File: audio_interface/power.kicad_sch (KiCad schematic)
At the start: 50 parts, among them J3 EXT_9V, J4 PROBE_GND, J5 EXT_5VA, J6 EXT_INV, J7 EXT_ANALOG, J8 D_PWR_SEL, J9 EXT_DIGITAL, U5 L4931, U6 LT1931, U7 TPS7A49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

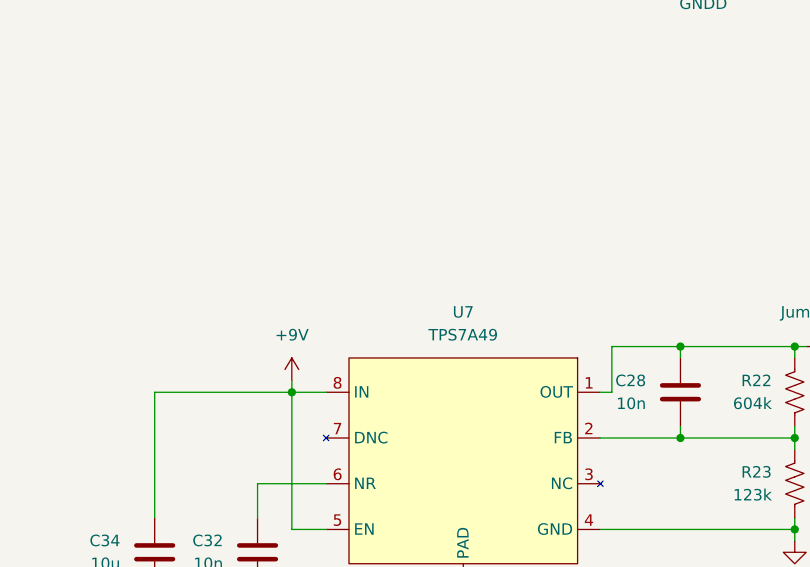
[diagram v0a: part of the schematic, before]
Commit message: Fixed some footprints, fixed silkscreen.
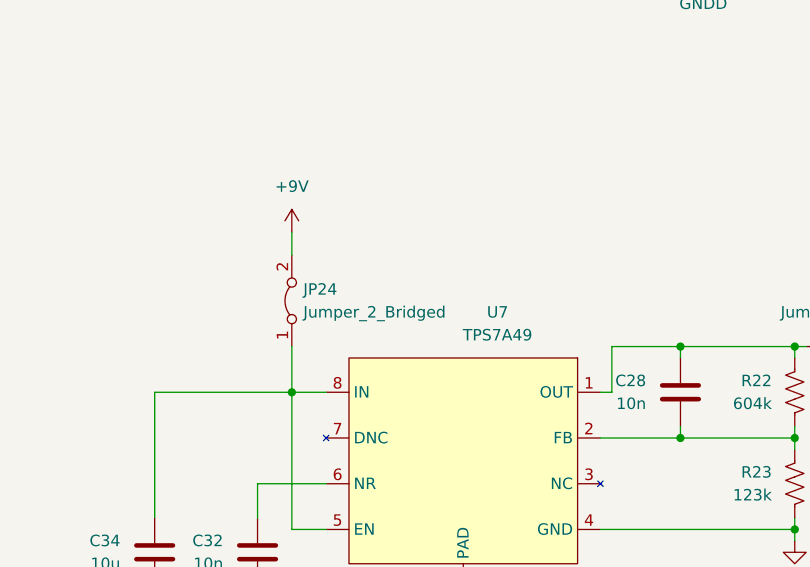
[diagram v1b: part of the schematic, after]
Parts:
- added JP24: Jumper_2_Bridged, Resistor_SMD:R_1206_3216Metric_Pad1.30x1.75mm_HandSolder, symbol Jumper:Jumper_2_Bridged
- J3: footprint Connector_BarrelJack:BarrelJack_CUI_PJ-063AH_Horizontal -> Connector_BarrelJack:BarrelJack_GCT_DCJ200-10-A_Horizontal
- TP8: footprint TestPoint:TestPoint_Loop_D2.54mm_Drill1.5mm_Beaded -> TestPoint:TestPoint_Loop_D2.50mm_Drill1.0mm
- U7, U8: footprint Package_SO:VSSOP-8_3.0x3.0mm_P0.65mm -> Package_SO:MSOP-8-1EP_3x3mm_P0.65mm_EP1.68x1.88mm_ThermalVias
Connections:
- net +9V: now also JP24.2 (B); no longer C34.1, U7.5 (EN), U7.8 (IN)
- new net: C34.1, JP24.1 (A), U7.5 (EN), U7.8 (IN)
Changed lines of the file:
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@@
+    (stroke (width 0) (type default) (color 0 0 0 0))
+  )
+  (wire (pts (xy 185.42 83.82) (xy 185.42 88.9))
     (stroke (width 0) (type default) (color 0 0 0 0))
   )
@@
     (stroke (width 0) (type default) (color 0 0 0 0))
   )
-  (wire (pts (xy 185.42 87.63) (xy 185.42 88.9))
-    (stroke (width 0) (type default) (color 0 0 0 0))
-  )
   (wire (pts (xy 87.63 33.02) (xy 92.71 33.02))
     (stroke (width 0) (type default) (color 0 0 0 0))
@@
   )
   (wire (pts (xy 185.42 104.14) (xy 189.23 104.14))
+    (stroke (width 0) (type default) (color 0 0 0 0))
+  )
+  (wire (pts (xy 185.42 71.12) (xy 185.42 73.66))
     (stroke (width 0) (type default) (color 0 0 0 0))
   )
@@
     (pin "1")
   )
+  (symbol (lib_id "Jumper:Jumper_2_Bridged") (at 185.42 78.74 90) (unit 1)
+    (in_bom yes) (on_board yes) (fields_autoplaced)
+    (property "Reference" "JP24" (id 0) (at 186.69 77.4699 90)
+      (effects (font (size 1.27 1.27)) (justify right))
+    )
+    (property "Value" "Jumper_2_Bridged" (id 1) (at 186.69 80.0099 90)
+      (effects (font (size 1.27 1.27)) (justify right))
+    )
+    (property "Footprint" "Resistor_SMD:R_1206_3216Metric_Pad1.30x1.75mm_HandSolder" (id 2) (at 185.42 78.74 0)
+      (effects (font (size 1.27 1.27)) hide)
+    )
+    (property "Datasheet" "~" (id 3) (at 185.42 78.74 0)
+      (effects (font (size 1.27 1.27)) hide)
+    )
+    (pin "1")
+    (pin "2")
+  )
   (symbol (lib_id "Jumper:Jumper_2_Bridged") (at 247.65 83.82 0) (mirror y) (unit 1)
     (in_bom yes) (on_board yes) (fields_autoplaced)
@@
     (property "Reference" "J3" (id 0) (at 20.32 22.86 0))
     (property "Value" "EXT_9V" (id 1) (at 20.32 25.4 0))
-    (property "Footprint" "Connector_BarrelJack:BarrelJack_CUI_PJ-063AH_Horizontal" (id 2) (at 21.59 32.766 0)
+    (property "Footprint" "Connector_BarrelJack:BarrelJack_GCT_DCJ200-10-A_Horizontal" (id 2) (at 21.59 32.766 0)
       (effects (font (size 1.27 1.27)) hide)
     )
@@
     (pin "2")
   )
-  (symbol (lib_id "power:+9V") (at 185.42 87.63 0) (mirror y) (unit 1)
-    (in_bom yes) (on_board yes) (fields_autoplaced)
-    (property "Reference" "#PWR053" (id 0) (at 185.42 91.44 0)
-      (effects (font (size 1.27 1.27)) hide)
-    )
-    (property "Value" "+9V" (id 1) (at 185.42 82.55 0))
-    (property "Footprint" "" (id 2) (at 185.42 87.63 0)
-      (effects (font (size 1.27 1.27)) hide)
-    )
-    (property "Datasheet" "" (id 3) (at 185.42 87.63 0)
+  (symbol (lib_id "power:+9V") (at 185.42 71.12 0) (mirror y) (unit 1)
+    (in_bom yes) (on_board yes) (fields_autoplaced)
+    (property "Reference" "#PWR053" (id 0) (at 185.42 74.93 0)
+      (effects (font (size 1.27 1.27)) hide)
+    )
+    (property "Value" "+9V" (id 1) (at 185.42 66.04 0))
+    (property "Footprint" "" (id 2) (at 185.42 71.12 0)
+      (effects (font (size 1.27 1.27)) hide)
+    )
+    (property "Datasheet" "" (id 3) (at 185.42 71.12 0)
       (effects (font (size 1.27 1.27)) hide)
     )
@@
     (property "Reference" "U8" (id 0) (at 204.47 124.46 0))
     (property "Value" "TPS7A30" (id 1) (at 204.47 127 0))
-    (property "Footprint" "Package_SO:VSSOP-8_3.0x3.0mm_P0.65mm" (id 2) (at 204.47 135.89 0)
+    (property "Footprint" "Package_SO:MSOP-8-1EP_3x3mm_P0.65mm_EP1.68x1.88mm_ThermalVias" (id 2) (at 204.47 135.89 0)
       (effects (font (size 1.27 1.27)) hide)
     )
@@
   )
   (symbol (lib_id "Customs:TPS7A49") (at 204.47 91.44 0) (mirror y) (unit 1)
-    (in_bom yes) (on_board yes) (fields_autoplaced)
-    (property "Reference" "U7" (id 0) (at 204.47 80.01 0))
-    (property "Value" "TPS7A49" (id 1) (at 204.47 82.55 0))
-    (property "Footprint" "Package_SO:VSSOP-8_3.0x3.0mm_P0.65mm" (id 2) (at 204.47 91.44 0)
+    (in_bom yes) (on_board yes)
+    (property "Reference" "U7" (id 0) (at 208.28 80.01 0))
+    (property "Value" "TPS7A49" (id 1) (at 208.28 82.55 0))
+    (property "Footprint" "Package_SO:MSOP-8-1EP_3x3mm_P0.65mm_EP1.68x1.88mm_ThermalVias" (id 2) (at 204.47 91.44 0)
       (effects (font (size 1.27 1.27)) hide)
     )
@@
       (effects (font (size 1.27 1.27)) (justify left))
     )
-    (property "Footprint" "TestPoint:TestPoint_Loop_D2.54mm_Drill1.5mm_Beaded" (id 2) (at 55.88 34.29 0)
-      (effects (font (size 1.27 1.27)) hide)
-    )
+    (property "Footprint" "TestPoint:TestPoint_Loop_D2.50mm_Drill1.0mm" (id 2) (at 55.88 34.29 0)
+      (effects (font (size 1.27 1.27)) hide)
+    )

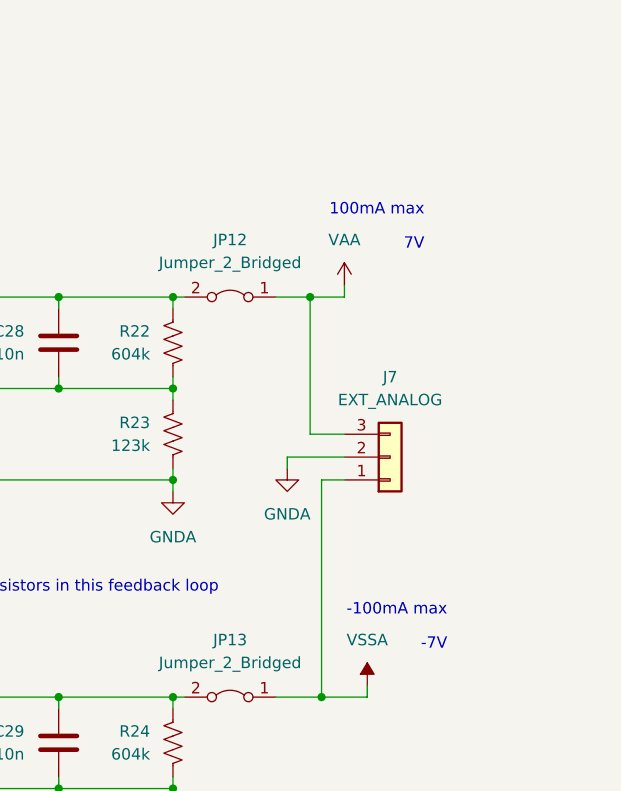
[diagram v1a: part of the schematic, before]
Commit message: Polygons for switching regulator. Silkscreen improvements,
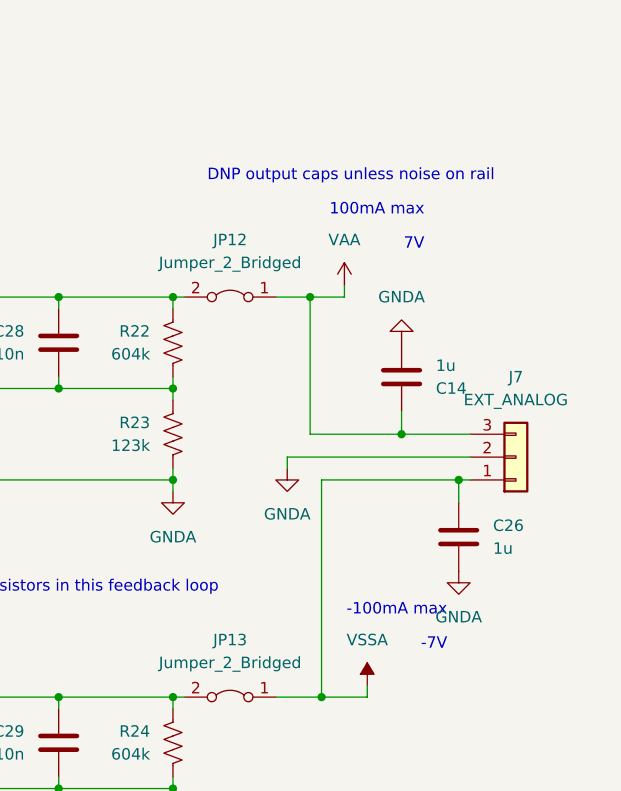
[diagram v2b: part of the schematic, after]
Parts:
- added C14, C26: 1u, Capacitor_SMD:C_1206_3216Metric_Pad1.33x1.80mm_HandSolder, symbol Device:C
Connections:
- net GNDA: now also C14.2, C26.2
- net VAA: now also C14.1
- net VSSA: now also C26.1
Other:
- note added: "DNP output caps unless noise on rail"
- moved on the sheet: J7
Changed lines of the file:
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@@
   (junction (at 90.17 172.72) (diameter 0) (color 0 0 0 0)
   )
+  (junction (at 266.7 99.06) (diameter 0) (color 0 0 0 0)
+  )
   (junction (at 101.6 163.83) (diameter 0) (color 0 0 0 0)
   )
@@
   (junction (at 210.82 26.67) (diameter 0) (color 0 0 0 0)
   )
+  (junction (at 273.05 104.14) (diameter 0) (color 0 0 0 0)
+  )
   (junction (at 241.3 104.14) (diameter 0) (color 0 0 0 0)
   )
@@
     (stroke (width 0) (type default) (color 0 0 0 0))
   )
-  (wire (pts (xy 260.35 104.14) (xy 257.81 104.14))
+  (wire (pts (xy 274.32 104.14) (xy 273.05 104.14))
     (stroke (width 0) (type default) (color 0 0 0 0))
   )
@@
     (stroke (width 0) (type default) (color 0 0 0 0))
   )
-  (wire (pts (xy 260.35 99.06) (xy 256.54 99.06))
+  (wire (pts (xy 274.32 99.06) (xy 266.7 99.06))
     (stroke (width 0) (type default) (color 0 0 0 0))
   )
@@
     (stroke (width 0) (type default) (color 0 0 0 0))
   )
+  (wire (pts (xy 273.05 104.14) (xy 257.81 104.14))
+    (stroke (width 0) (type default) (color 0 0 0 0))
+  )
   (wire (pts (xy 228.6 137.16) (xy 228.6 138.43))
     (stroke (width 0) (type default) (color 0 0 0 0))
@@
     (stroke (width 0) (type default) (color 0 0 0 0))
   )
-  (wire (pts (xy 254 101.6) (xy 260.35 101.6))
+  (wire (pts (xy 254 101.6) (xy 274.32 101.6))
     (stroke (width 0) (type default) (color 0 0 0 0))
   )
@@
     (stroke (width 0) (type default) (color 0 0 0 0))
   )
+  (wire (pts (xy 273.05 104.14) (xy 273.05 106.68))
+    (stroke (width 0) (type default) (color 0 0 0 0))
+  )
   (wire (pts (xy 228.6 93.98) (xy 219.71 93.98))
     (stroke (width 0) (type default) (color 0 0 0 0))
@@
     (stroke (width 0) (type default) (color 0 0 0 0))
   )
+  (wire (pts (xy 266.7 99.06) (xy 256.54 99.06))
+    (stroke (width 0) (type default) (color 0 0 0 0))
+  )
   (wire (pts (xy 87.63 24.13) (xy 87.63 33.02))
     (stroke (width 0) (type default) (color 0 0 0 0))
@@
   )
   (wire (pts (xy 220.98 88.9) (xy 220.98 83.82))
+    (stroke (width 0) (type default) (color 0 0 0 0))
+  )
+  (wire (pts (xy 266.7 99.06) (xy 266.7 96.52))
     (stroke (width 0) (type default) (color 0 0 0 0))
   )
@@
   (text "100mA max" (at 269.24 74.93 180)
     (effects (font (size 1.27 1.27)) (justify right bottom))
+  )
+  (text "DNP output caps unless noise on rail" (at 245.11 71.12 0)
+    (effects (font (size 1.27 1.27)) (justify left bottom))
   )
   (text "Allows for testing USB without bench supply" (at 163.83 35.56 0)
@@
     (pin "2")
   )
+  (symbol (lib_id "power:GNDA") (at 266.7 88.9 0) (mirror x) (unit 1)
+    (in_bom yes) (on_board yes) (fields_autoplaced)
+    (property "Reference" "#PWR0101" (id 0) (at 266.7 82.55 0)
+      (effects (font (size 1.27 1.27)) hide)
+    )
+    (property "Value" "GNDA" (id 1) (at 266.7 83.82 0))
+    (property "Footprint" "" (id 2) (at 266.7 88.9 0)
+      (effects (font (size 1.27 1.27)) hide)
+    )
+    (property "Datasheet" "" (id 3) (at 266.7 88.9 0)
+      (effects (font (size 1.27 1.27)) hide)
+    )
+    (pin "1")
+  )
   (symbol (lib_id "power:GNDA") (at 241.3 149.86 0) (mirror y) (unit 1)
     (in_bom yes) (on_board yes) (fields_autoplaced)
@@
     (pin "1")
   )
+  (symbol (lib_id "Device:C") (at 273.05 110.49 0) (unit 1)
+    (in_bom yes) (on_board yes) (fields_autoplaced)
+    (property "Reference" "C26" (id 0) (at 276.86 109.2199 0)
+      (effects (font (size 1.27 1.27)) (justify left))
+    )
+    (property "Value" "1u" (id 1) (at 276.86 111.7599 0)
+      (effects (font (size 1.27 1.27)) (justify left))
+    )
+    (property "Footprint" "Capacitor_SMD:C_1206_3216Metric_Pad1.33x1.80mm_HandSolder" (id 2) (at 274.0152 114.3 0)
+      (effects (font (size 1.27 1.27)) hide)
+    )
+    (property "Datasheet" "~" (id 3) (at 273.05 110.49 0)
+      (effects (font (size 1.27 1.27)) hide)
+    )
+    (pin "1")
+    (pin "2")
+  )
   (symbol (lib_id "Customs:L4931") (at 231.14 27.94 0) (unit 1)
     (in_bom yes) (on_board yes) (fields_autoplaced)
@@
     (pin "2")
   )
+  (symbol (lib_id "Device:C") (at 266.7 92.71 0) (mirror x) (unit 1)
+    (in_bom yes) (on_board yes) (fields_autoplaced)
+    (property "Reference" "C14" (id 0) (at 270.51 93.9801 0)
+      (effects (font (size 1.27 1.27)) (justify left))
+    )
+    (property "Value" "1u" (id 1) (at 270.51 91.4401 0)
+      (effects (font (size 1.27 1.27)) (justify left))
+    )
+    (property "Footprint" "Capacitor_SMD:C_1206_3216Metric_Pad1.33x1.80mm_HandSolder" (id 2) (at 267.6652 88.9 0)
+      (effects (font (size 1.27 1.27)) hide)
+    )
+    (property "Datasheet" "~" (id 3) (at 266.7 92.71 0)
+      (effects (font (size 1.27 1.27)) hide)
+    )
+    (pin "1")
+    (pin "2")
+  )
   (symbol (lib_id "power:GNDA") (at 204.47 110.49 0) (mirror y) (unit 1)
     (in_bom yes) (on_board yes) (fields_autoplaced)
@@
     (pin "2")
   )
-  (symbol (lib_id "Connector_Generic:Conn_01x03") (at 265.43 101.6 0) (mirror x) (unit 1)
-    (in_bom yes) (on_board yes) (fields_autoplaced)
-    (property "Reference" "J7" (id 0) (at 265.43 92.71 0))
-    (property "Value" "EXT_ANALOG" (id 1) (at 265.43 95.25 0))
-    (property "Footprint" "Connector_PinHeader_2.54mm:PinHeader_1x03_P2.54mm_Vertical" (id 2) (at 265.43 101.6 0)
-      (effects (font (size 1.27 1.27)) hide)
-    )
-    (property "Datasheet" "~" (id 3) (at 265.43 101.6 0)
+  (symbol (lib_id "Connector_Generic:Conn_01x03") (at 279.4 101.6 0) (mirror x) (unit 1)
+    (in_bom yes) (on_board yes) (fields_autoplaced)
+    (property "Reference" "J7" (id 0) (at 279.4 92.71 0))
+    (property "Value" "EXT_ANALOG" (id 1) (at 279.4 95.25 0))
+    (property "Footprint" "Connector_PinHeader_2.54mm:PinHeader_1x03_P2.54mm_Vertical" (id 2) (at 279.4 101.6 0)
+      (effects (font (size 1.27 1.27)) hide)
+    )
+    (property "Datasheet" "~" (id 3) (at 279.4 101.6 0)
       (effects (font (size 1.27 1.27)) hide)
     )
@@
     (pin "2")
   )
+  (symbol (lib_id "power:GNDA") (at 273.05 114.3 0) (unit 1)
+    (in_bom yes) (on_board yes) (fields_autoplaced)
+    (property "Reference" "#PWR0103" (id 0) (at 273.05 120.65 0)
+      (effects (font (size 1.27 1.27)) hide)
+    )
+    (property "Value" "GNDA" (id 1) (at 273.05 119.38 0))
+    (property "Footprint" "" (id 2) (at 273.05 114.3 0)
+      (effects (font (size 1.27 1.27)) hide)
+    )
+    (property "Datasheet" "" (id 3) (at 273.05 114.3 0)
+      (effects (font (size 1.27 1.27)) hide)
+    )
+    (pin "1")
+  )
   (symbol (lib_id "Customs:L4931") (at 66.04 87.63 0) (unit 1)
